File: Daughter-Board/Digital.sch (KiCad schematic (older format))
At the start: 28 parts, among them J201 302-S101, U102 MC74VHCT126A, U201 74HC540, U202 PIC32MZ2048EFM064-TQFP

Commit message: Add test points to Digital and Daughter-Board schematics
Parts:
- added TP201, TP202, TP203, TP204, TP211, TP212, TP213, TP214, TP215, TP216, TP217, TP218, TP219, TP220, TP221, TP222, TP223, TP224, TP225: 5000, digikey-footprints:Test_Point_D1.02mm, symbol dk_Test-Points:5000
- gave numbers to parts that had none: 6
- renumbered D208 to D201, D207 to D202, D206 to D203, D205 to D204, D204 to D205, D203 to D206, D202 to D207, D201 to D208, R208 to R201, R207 to R202, R206 to R203, R205 to R204, R204 to R205, R203 to R206, R202 to R207, R201 to R208, U102 to U106
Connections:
- net AOut_1: now also TP213.1
- net AOut_2: now also TP214.1
- net AOut_3: now also TP215.1
- net AOut_4: now also TP216.1
- net CLK_EN: now also TP212.1
- net DOut: now also TP211.1
- net DOut_EN_1: now also TP217.1
- net DOut_EN_4: no longer U202.30 (~SS3~/AN10/RB15), U202.43 (~SS4~/SDA1/RD9)
- net MB_Comm_En: now also TP218.1
- net MST_CLK: now also TP219.1
- net NegEn: now also TP203.1
- net No_Gain: now also TP201.1
- net PlusEn: now also TP204.1
- net Plus_GND: now also TP202.1
- net Select: now also TP221.1
- net at J201.2, U202.23 (TMS/AN5/RB10): now also TP224.1
- net at J201.6, U202.24 (TDO/AN6/RB11): now also TP222.1
- net at J201.4, U202.27 (TCK/AN7/RB12): now also TP225.1
- net at J201.8, U202.28 (TDI/AN8/RB13): now also TP223.1
- net Word_Select renamed Word_Strobe
- net Word_Strobe: now also U202.30 (~SS3~/AN10/RB15), U202.43 (~SS4~/SDA1/RD9), TP220.1

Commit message: Add DigiKey # or Mouser # to component info, update footprintinfo for 14 and 20 pin devices.
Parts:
- C201: DigiKey # (none) -> 476-12852-1-ND
- D201: DigiKey 754-1944-1-ND -> (none); DigiKey # (none) -> 754-1944-1-ND
- J201: Category Connectors, Interconnects -> (none); DK_Datasheet_Link http://www.on-shore.com/wp-content/uploads/2018/04/302-SXX1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 -> (none); DK_Detail_Page /product-detail/en/on-shore-technology-inc/302-S101/ED1543-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 -> (none); Description CONN HEADER VERT 10POS 2.54MM -> (none); Digi-Key_PN ED1543-ND -> (none); DigiKey # (none) -> ED1543-ND; Family Rectangular Connectors - Headers, Male Pins -> (none); MPN 302-S101 -> (none); Manufacturer On Shore Technology Inc. -> (none); Status Active -> (none)
- R201: DigiKey # (none) -> 541-CRCW12061K00FKEBCCT-ND
- R202, R203, R204, R205, R206, R207, R208: DigiKey # (none) -> 541-CRCW12061K00FKEBCCT
- R209: DigiKey # (none) -> 541-CRCW12063K90FKEACCT-ND
- U106: Mouser # (none) -> 771-74VHCT126D118
- U201: DigiKey 1727-3320-ND -> (none); DigiKey # (none) -> 1727-3320-ND
- U202: DigiKey # (none) -> PIC32MZ2048EFM064-E/PT-ND
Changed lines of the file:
@@
 F 2 "Package_SO:SOIC-14_3.9x8.7mm_P1.27mm" H 8240 3900 50  0001 C CNN
 F 3 "" H 8240 3900 50  0001 C CNN
+F 4 "771-74VHCT126D118" H 8240 3900 50  0001 C CNN "Mouser #"
 	1    8240 3900
 	-1   0    0    -1
@@
 F 2 "Package_SO:SOIC-14_3.9x8.7mm_P1.27mm" H 8040 2300 50  0001 C CNN
 F 3 "" H 8040 2300 50  0001 C CNN
+F 4 "771-74VHCT126D118" H 8040 2300 50  0001 C CNN "Mouser #"
 	2    8040 2300
 	-1   0    0    -1
@@
 F 2 "Package_SO:SOIC-14_3.9x8.7mm_P1.27mm" H 8240 6200 50  0001 C CNN
 F 3 "" H 8240 6200 50  0001 C CNN
+F 4 "771-74VHCT126D118" H 8240 6200 50  0001 C CNN "Mouser #"
 	3    8240 6200
 	-1   0    0    -1
@@
 F 2 "Package_SO:SOIC-14_3.9x8.7mm_P1.27mm" H 8240 5000 50  0001 C CNN
 F 3 "" H 8240 5000 50  0001 C CNN
+F 4 "771-74VHCT126D118" H 8240 5000 50  0001 C CNN "Mouser #"
 	4    8240 5000
 	-1   0    0    1
@@
 F 2 "digikey-footprints:PinHeader_2x5_P2.54mm_Drill1.2mm" H 5240 7300 60  0001 L CNN
 F 3 "http://www.on-shore.com/wp-content/uploads/2018/04/302-SXX1.pdf" V 5240 7400 60  0001 L CNN
-F 4 "ED1543-ND" H 5240 7500 60  0001 L CNN "Digi-Key_PN"
-F 5 "302-S101" H 5240 7600 60  0001 L CNN "MPN"
-F 6 "Connectors, Interconnects" H 5240 7700 60  0001 L CNN "Category"
-F 7 "Rectangular Connectors - Headers, Male Pins" H 5240 7800 60  0001 L CNN "Family"
-F 8 "http://www.on-shore.com/wp-content/uploads/2018/04/302-SXX1.pdf" H 5240 7900 60  0001 L CNN "DK_Datasheet_Link"
-F 9 "/product-detail/en/on-shore-technology-inc/302-S101/ED1543-ND/2178422" H 5240 8000 60  0001 L CNN "DK_Detail_Page"
-F 10 "CONN HEADER VERT 10POS 2.54MM" H 5240 8100 60  0001 L CNN "Description"
-F 11 "On Shore Technology Inc." H 5240 8200 60  0001 L CNN "Manufacturer"
-F 12 "Active" H 5240 8300 60  0001 L CNN "Status"
+F 4 "ED1543-ND" H 5240 7500 60  0001 L CNN "DigiKey #"
 	1    5040 7100
 	1    0    0    -1
@@
 F 2 "Resistor_SMD:R_1206_3216Metric_Pad1.30x1.75mm_HandSolder" V 3580 7040 50  0001 C CNN
 F 3 "~" H 3540 7050 50  0001 C CNN
+F 4 "541-CRCW12063K90FKEACCT-ND" H 3540 7050 50  0001 C CNN "DigiKey #"
 	1    3540 7050
 	1    0    0    -1
@@
 F 2 "Capacitor_SMD:C_1206_3216Metric" H 3578 7350 50  0001 C CNN
 F 3 "~" H 3540 7500 50  0001 C CNN
+F 4 "476-12852-1-ND" H 3540 7500 50  0001 C CNN "DigiKey #"
 	1    3540 7500
 	1    0    0    -1
@@
 F 2 "Package_SO:TSSOP-20_4.4x6.5mm_P0.65mm" H 4800 1500 50  0001 C CNN
 F 3 "" H 4800 1500 50  0001 C CNN
-F 4 "1727-3320-ND" H 4800 1500 50  0001 C CNN "DigiKey"
+F 4 "1727-3320-ND" H 4800 1500 50  0001 C CNN "DigiKey #"
 	1    4800 1500
 	-1   0    0    -1
@@
 F 2 "Resistor_SMD:R_1206_3216Metric_Pad1.30x1.75mm_HandSolder" V 3190 690 50  0001 C CNN
 F 3 "~" H 3150 700 50  0001 C CNN
-F 4 "" V 3150 700 50  0001 C CNN "DigiKey"
+F 4 "541-CRCW12061K00FKEBCCT-ND" V 3150 700 50  0001 C CNN "DigiKey #"
 	1    3150 700
 	0    1    1    0
@@
 F 2 "Resistor_SMD:R_1206_3216Metric_Pad1.30x1.75mm_HandSolder" V 3190 1090 50  0001 C CNN
 F 3 "~" H 3150 1100 50  0001 C CNN
+F 4 "541-CRCW12061K00FKEBCCT" V 3150 1100 50  0001 C CNN "DigiKey #"
 	1    3150 1100
 	0    1    1    0
@@
 F 2 "Resistor_SMD:R_1206_3216Metric_Pad1.30x1.75mm_HandSolder" V 3190 1490 50  0001 C CNN
 F 3 "~" H 3150 1500 50  0001 C CNN
+F 4 "541-CRCW12061K00FKEBCCT" V 3150 1500 50  0001 C CNN "DigiKey #"
 	1    3150 1500
 	0    1    1    0
@@
 F 2 "Resistor_SMD:R_1206_3216Metric_Pad1.30x1.75mm_HandSolder" V 3190 1890 50  0001 C CNN
 F 3 "~" H 3150 1900 50  0001 C CNN
+F 4 "541-CRCW12061K00FKEBCCT" V 3150 1900 50  0001 C CNN "DigiKey #"
 	1    3150 1900
 	0    1    1    0
@@
 F 2 "Resistor_SMD:R_1206_3216Metric_Pad1.30x1.75mm_HandSolder" V 3190 890 50  0001 C CNN
 F 3 "~" H 3150 900 50  0001 C CNN
+F 4 "541-CRCW12061K00FKEBCCT" V 3150 900 50  0001 C CNN "DigiKey #"
 	1    3150 900
 	0    1    1    0
@@
 F 2 "Resistor_SMD:R_1206_3216Metric_Pad1.30x1.75mm_HandSolder" V 3190 1290 50  0001 C CNN
 F 3 "~" H 3150 1300 50  0001 C CNN
+F 4 "541-CRCW12061K00FKEBCCT" V 3150 1300 50  0001 C CNN "DigiKey #"
 	1    3150 1300
 	0    1    1    0
@@
 F 2 "Resistor_SMD:R_1206_3216Metric_Pad1.30x1.75mm_HandSolder" V 3190 1690 50  0001 C CNN
 F 3 "~" H 3150 1700 50  0001 C CNN
+F 4 "541-CRCW12061K00FKEBCCT" V 3150 1700 50  0001 C CNN "DigiKey #"
 	1    3150 1700
 	0    1    1    0
@@
 F 2 "Resistor_SMD:R_1206_3216Metric_Pad1.30x1.75mm_HandSolder" V 3190 2090 50  0001 C CNN
 F 3 "~" H 3150 2100 50  0001 C CNN
+F 4 "541-CRCW12061K00FKEBCCT" V 3150 2100 50  0001 C CNN "DigiKey #"
 	1    3150 2100
 	0    1    1    0
@@
 F 2 "LED_SMD:LED_1206_3216Metric_Pad1.42x1.75mm_HandSolder" H 2650 700 50  0001 C CNN
 F 3 "~" H 2650 700 50  0001 C CNN
-F 4 "754-1944-1-ND" H 2650 700 50  0001 C CNN "DigiKey"
+F 4 "754-1944-1-ND" H 2650 700 50  0001 C CNN "DigiKey #"
 	1    2650 700
 	-1   0    0    -1
@@
 F 2 "Package_QFP:TQFP-64_10x10mm_P0.5mm" H 5840 4350 50  0001 C CNN
 F 3 "" H 5840 4350 50  0001 C CNN
+F 4 "PIC32MZ2048EFM064-E/PT-ND" H 5840 4350 50  0001 C CNN "DigiKey #"
 	1    5840 4350
 	1    0    0    -1

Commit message: Corrected analog gain switch position.
Analog gain switch was across the feedback resistor. It is changed to grounding of the - input resistor to the op amp.
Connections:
- net No_Gain renamed SingleGain
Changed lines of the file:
@@
 Plus_GND
 Text HLabel 2120 2900 0    50   Output ~ 0
-No_Gain
+SingleGain
 Text HLabel 10000 4300 2    50   Output ~ 0
 CLK_EN

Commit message: Remove LEDs and circuitry, update J201 footprint to have a square pad on pin 1.]
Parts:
- removed D201, D202, D203, D204, D205, D206, D207, D208: LED_ALT, LED_SMD:LED_1206_3216Metric_Pad1.42x1.75mm_HandSolder, symbol Device:LED_ALT
- removed R201, R202, R203, R204, R205, R206, R207, R208: 1.0K, Resistor_SMD:R_1206_3216Metric_Pad1.30x1.75mm_HandSolder, symbol Device:R_US
- removed U201: 74HC540, Package_SO:TSSOP-20_4.4x6.5mm_P0.65mm, symbol 74xx:74LS540
- R209: value 3.9K -> 10K
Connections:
- net Mic1: no longer names the net of U202.52 (RD4)
- net Mic2: no longer names the net of U202.53 (RD5)
- net Mic3: no longer names the net of U202.56 (RF0)
- net Mic4: no longer names the net of U202.57 (RF1)
- no-connect marks 13 -> 17

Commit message: Add connector for PICkit to MCU interface.
In the process of adding the PICkit connector some control lines had to be moved.
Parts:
- removed U202: PIC32MZ2048EFM064-TQFP, Package_QFP:TQFP-64_10x10mm_P0.5mm, symbol dcm-symbols:PIC32MZ2048EFM064-TQFP
- added J202: TSW-108-09-G-S-RA, SAMTEC_TSW-108-09-G-S-RA, symbol TSW-108-09-G-S-RA:TSW-108-09-G-S-RA
- added TP226, TP227, TP228, TP229, TP230: 5000, digikey-footprints:Test_Point_D1.02mm, symbol dk_Test-Points:5000
- added U201: PIC32MZ2048EFM064-TQFP, Package_QFP:TQFP-64_10x10mm_P0.5mm, symbol dcm-symbols:PIC32MZ2048EFM064-TQFP
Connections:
- net +5V: now also J202.02, TP229.1, U201.19 (AVdd), U201.26 (Vdd), U201.39 (Vdd), U201.54 (Vdd), U201.60 (Vdd), U201.8 (Vdd)
- net AOut_1: now also U201.14 (AN2/RB2)
- net AOut_2: now also U201.13 (AN3/RB3)
- net AOut_3: now also U201.12 (AN4/RB4)
- net AOut_4: now also TP217.1, U201.10 (~SS2~/AN11/RG9); no longer TP216.1
- net CLK_EN: now also U201.41 (RF4)
- net Clk_Out: now also U201.4 (SCK2/AN14/RG6)
- net DOut_EN_1: now also TP216.1, U201.11 (RB5); no longer TP217.1
- net DOut_EN_2: now also U201.6 (AN12/RG8)
- net DOut_EN_3: now also U201.3 (AN15/RE7)
- net DOut_EN_4: now also U201.2 (AN16/RE6)
- net Data_In: now also U201.1 (SDI2/AN17/RE5)
- net Data_Out: now also U201.5 (SDO2/AN13/RG7)
- net GNDREF: now also J201.3, J201.5, J201.9, J202.03, TP230.1, U201.20 (AVss), U201.25 (Vss), U201.35 (Vss), U201.40 (Vss), U201.55 (Vss), U201.59 (Vss), U201.7 (Vss)
- net MB_Comm_En: now also U201.58 (RE0)
- net NegEn: now also U201.62 (RE2)
- net PlusEn: now also U201.61 (RE1)
- net Plus_GND: now also U201.63 (RE3)
- net Select: now also U201.53 (RD5)
- net SingleGain: now also U201.64 (AN18/RE4)
- net Word_Strobe: now also U201.30 (~SS3~/AN10/RB15), U201.43 (~SS4~/SDA1/RD9), U201.52 (RD4)
- net at U106.10: now also U201.21 (RB8)
- net SPI: now reaches U106.8
- net SPI: now also U201.22 (SDI3/RB9)
- net TMS: now reaches J201.2, TP224.1
- net TMS: now also U201.23 (TMS/AN5/RB10)
- net TDO: now reaches J201.6, TP222.1
- net TDO: now also U201.24 (TDO/AN6/RB11)
- net TCK: now reaches J201.4, TP225.1
- net TCK: now also U201.27 (TCK/AN7/RB12)
- net TDI: now reaches J201.8, TP223.1
- net TDI: now also U201.28 (TDI/AN8/RB13)
- net MCLK: now reaches U106.11
- net MCLK: now also U201.29 (AN9/RB14), U201.44 (SCK4/RD10), U201.51 (SCL3/RD3)
- net at U106.1: now also U201.42 (RF5)
- net I2S: now reaches U106.3
- net I2S: now also U201.45 (SDI4/RD11)
- net at U106.4: now also U201.49 (SCK1/RD1)
- net I2C: now reaches U106.6
- net I2C: now also U201.50 (SDA3/RD2)
- net ~MCLR: now reaches C201.1, J201.10, R209.2
- net ~MCLR: now also J202.01, TP226.1, U201.9 (~MCLR)
- new net PGC: J202.05, TP228.1, U201.15 (AN1/RB1)
- new net PGD: J202.04, TP227.1, U201.16 (AN0/RB0)
- no-connect marks 17 -> 18
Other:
- note removed: "I2C"
- note removed: "I2S"
- note removed: "SPI"
- moved on the sheet: TP201, TP202, TP203, TP204, TP218, TP220, TP221

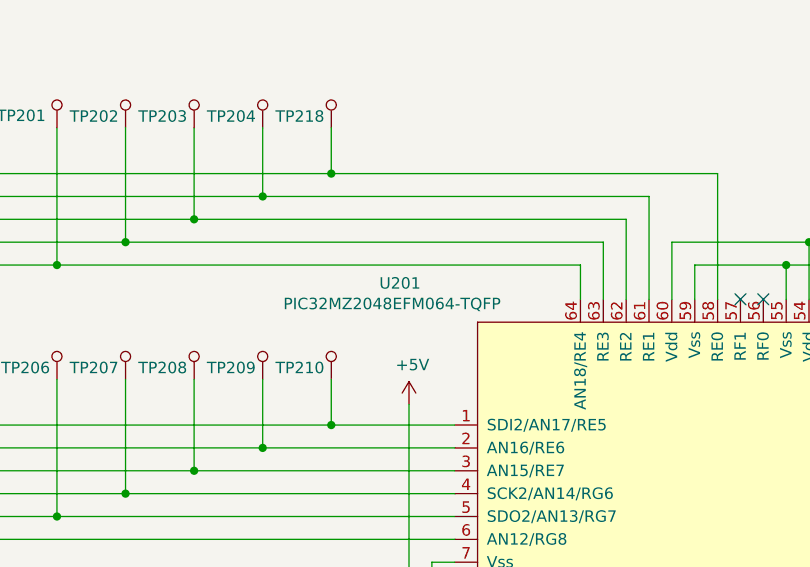
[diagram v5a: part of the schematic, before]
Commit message: Modify schematic to recover PCB layout.
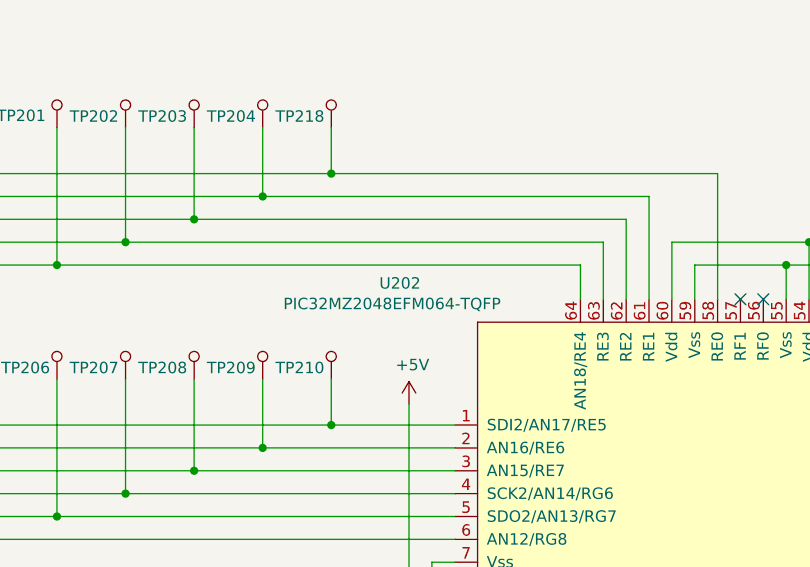
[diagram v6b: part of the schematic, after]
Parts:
- C201: footprint Capacitor_SMD:C_1206_3216Metric -> Capacitor_SMD:C_0805_2012Metric
- R209: footprint Resistor_SMD:R_1206_3216Metric_Pad1.30x1.75mm_HandSolder -> Resistor_SMD:R_0805_2012Metric
- TP201, TP202, TP203, TP204, TP205, TP206, TP207, TP208, TP209, TP210, TP211, TP212, TP213, TP214, TP215, TP216, TP217, TP218, TP219, TP220, TP221, TP222, TP223, TP224, TP225, TP226, TP227, TP228, TP229, TP230: footprint digikey-footprints:Test_Point_D1.02mm -> TestPoint:TestPoint_Pad_D1.0mm
- U106: Mouser # 771-74VHCT126D118 -> (none)
- renumbered U201 to U202
